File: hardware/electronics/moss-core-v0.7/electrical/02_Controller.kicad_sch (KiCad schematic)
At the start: 27 parts, among them SW1 RESET_N, SW2 BOOT_N, U1 ESP32-S3-WROOM-1U-N8, U20 TPS3808G33DBVR

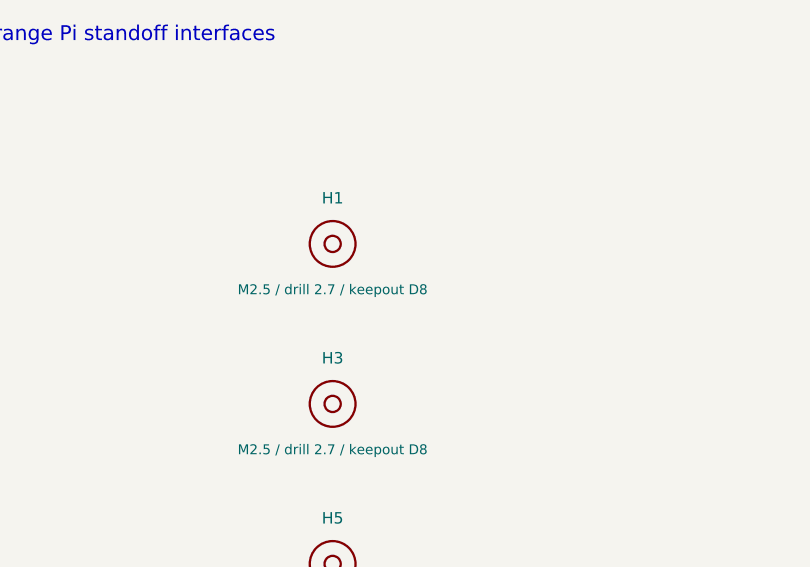
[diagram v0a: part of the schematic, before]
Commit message: Update MOSS Core V0.7 prototype files for 31 October
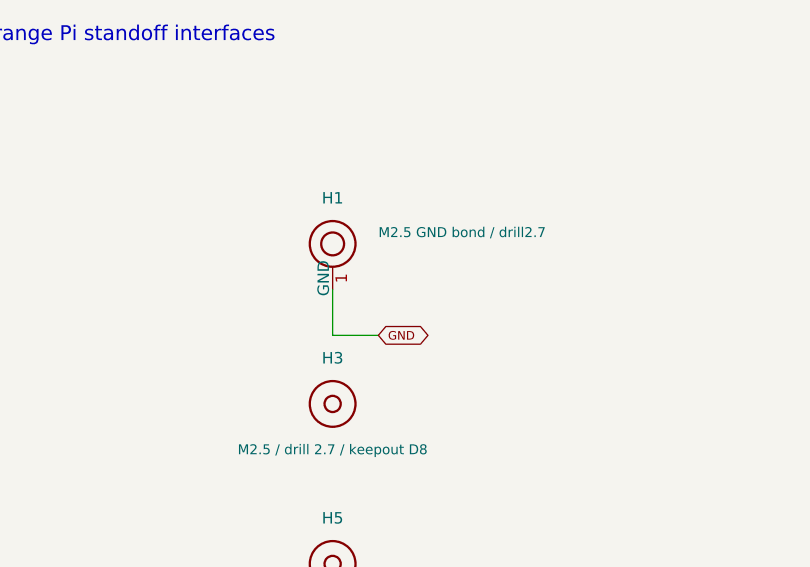
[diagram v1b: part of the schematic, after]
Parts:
- H1: value M2.5 / drill 2.7 / keepout D8 -> M2.5 GND bond / drill2.7; footprint MOSS:MOSS_Mount_M2p5_2p7_D8 -> MOSS:MOSS_Mount_M2p5_GND_D8; symbol MOSS:H1_M2_5___drill_2_7___keepout_D8 -> MOSS:H1_M2p5_GND_bond; MPN NPTH -> PCB_FEATURE
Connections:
- net GND: now also H1.1 (GND)
